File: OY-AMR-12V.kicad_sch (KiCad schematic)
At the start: 23 parts, among them J1 34696-0100, K1 FBR51NL210-W1-RW, K2 FBR51ND12-W1, K3 FBR51ND12-W1, K4 FBR56ND12-W, K5 FBR56ND12-W, K6 ACNH3212

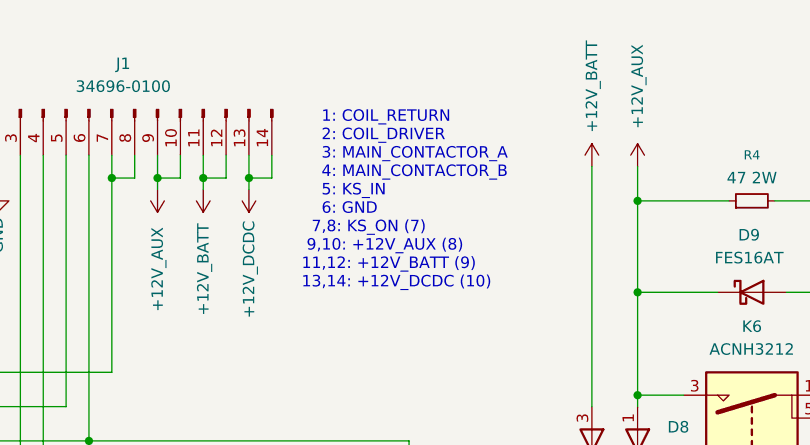
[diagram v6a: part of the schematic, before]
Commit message: Update connector text annotation
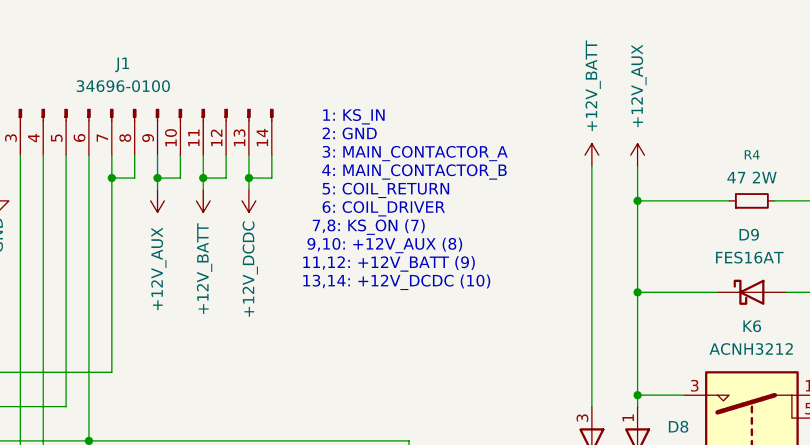
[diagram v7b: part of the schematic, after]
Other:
- note added: "1: KS_IN 2: GND 3: MAIN_CONTACTOR_A 4: MAIN_CONTACTOR_B 5: COIL_RETURN 6: COIL_DRIVER 7,8: KS_ON (7) 9,10: +12V_AUX (8) 11,12: +12V_BATT (9) 13,14: +12V_DCDC (10)"
- note removed: "1: COIL_RETURN 2: COIL_DRIVER 3: MAIN_CONTACTOR_A 4: MAIN_CONTACTOR_B 5: KS_IN 6: GND 7,8: KS_ON (7) 9,10: +12V_AUX (8) 11,12: +12V_BATT (9) 13,14: +12V_DCDC (10)"
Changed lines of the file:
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@@
 	(generator_version "9.0")
 	(paper "A4")
-	(text "    1: COIL_RETURN\n    2: COIL_DRIVER\n    3: MAIN_CONTACTOR_A\n    4: MAIN_CONTACTOR_B\n    5: KS_IN\n    6: GND\n  7,8: KS_ON (7)\n 9,10: +12V_AUX (8)\n11,12: +12V_BATT (9)\n13,14: +12V_DCDC (10)"
+	(text "    1: KS_IN\n    2: GND\n    3: MAIN_CONTACTOR_A\n    4: MAIN_CONTACTOR_B\n    5: COIL_RETURN\n    6: COIL_DRIVER\n  7,8: KS_ON (7)\n 9,10: +12V_AUX (8)\n11,12: +12V_BATT (9)\n13,14: +12V_DCDC (10)"
 		(exclude_from_sim no)
 		(at 196.342 50.546 0)
